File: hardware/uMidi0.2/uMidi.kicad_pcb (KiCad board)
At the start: 2 copper layers, 76.2 x 43.2 mm, 43 parts, among them CON1 USB-MINI-B, IC1 6N138, IC2 ATXMEGA128A4U-M, P1 MIDI In, P2 MIDI Thru, P3 MIDI T/O, P4 MIDI Out, P5 5..12 V, P6 PDI, P7 GPIO1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

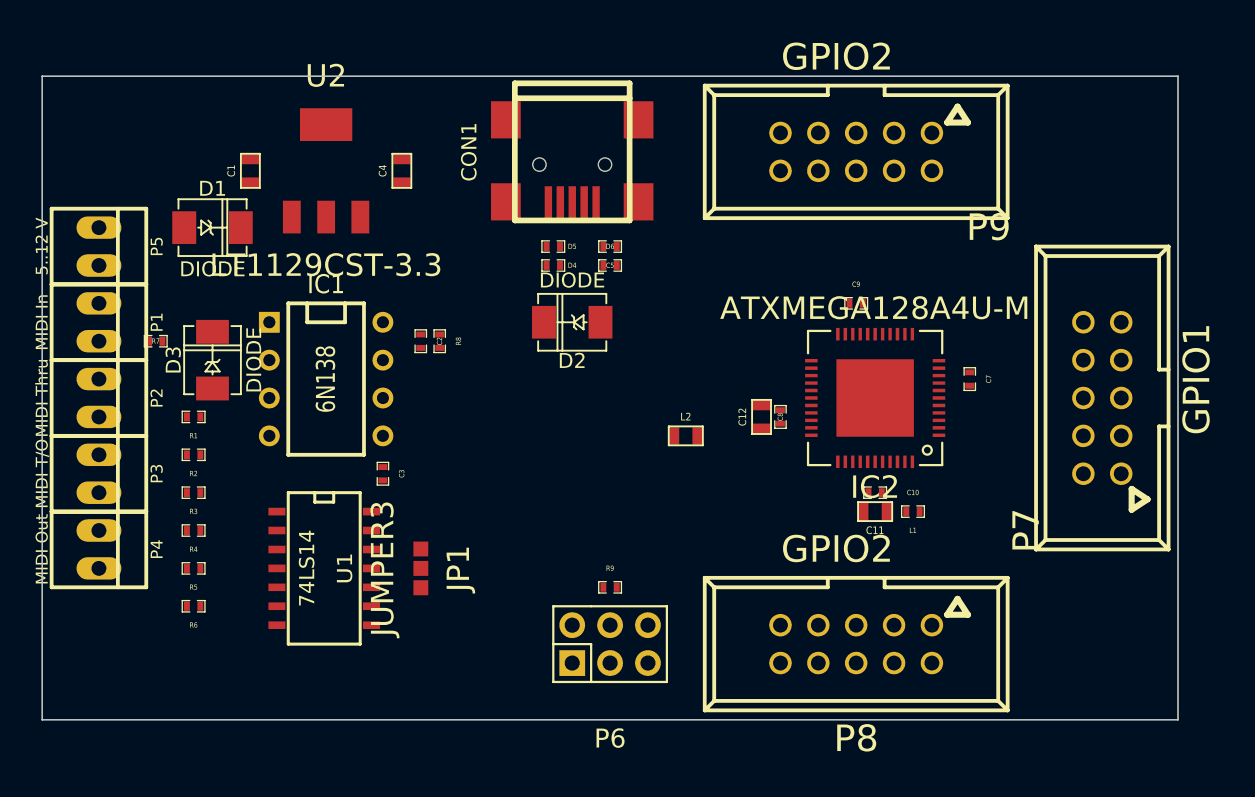
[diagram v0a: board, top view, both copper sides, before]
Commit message: Revise placement, make more compact
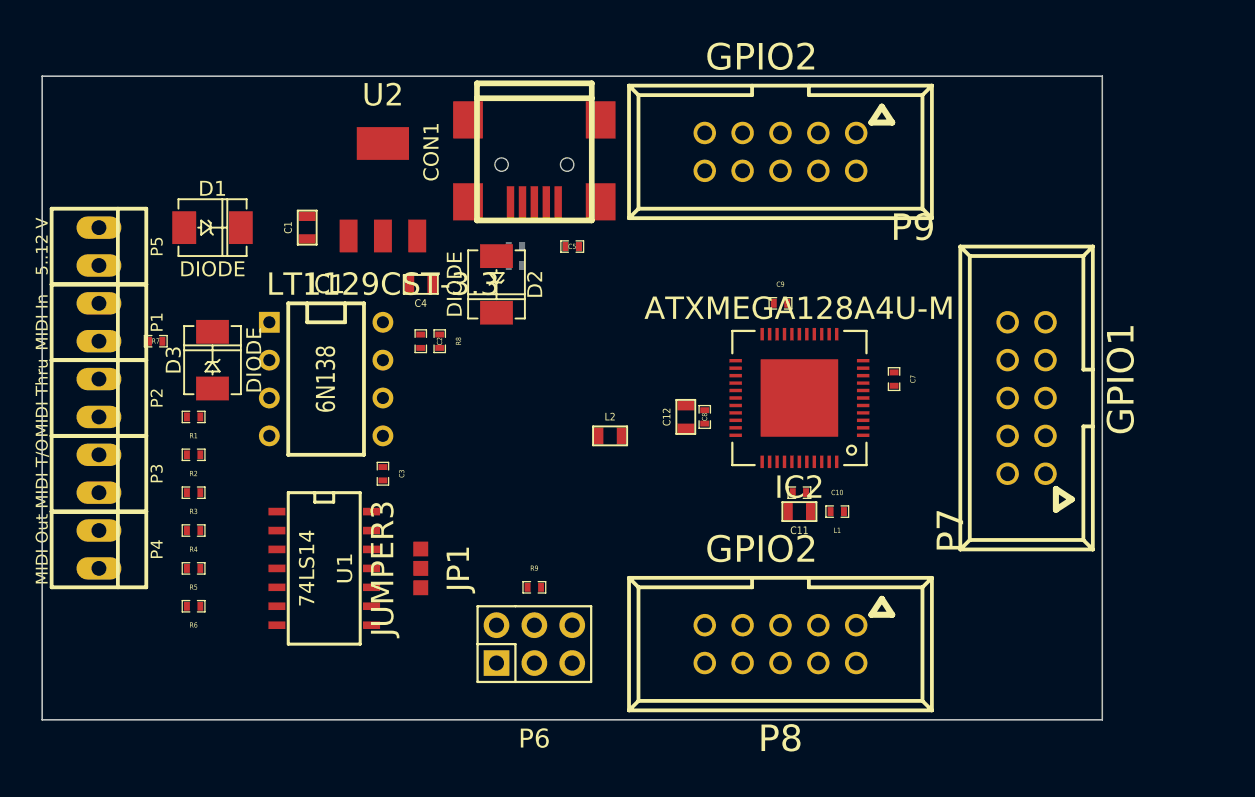
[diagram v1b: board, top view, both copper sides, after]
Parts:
- D4, D5, D6: moved to B.Cu
- moved C4 7.73 mm to (92.7, 135.9), turned to 180 degrees
- moved D2 5.68 mm to (97.8, 135.9), turned to 270 degrees
- moved C1 5.39 mm to (85.1, 132.1)
- moved P7 5.08 mm to (133.3, 143.5)
- moved C10 5.08 mm to (118.1, 149.9)
- moved C11 5.08 mm to (118.1, 151.1)
- moved C12 5.08 mm to (110.5, 144.8)
- moved C7 5.08 mm to (124.5, 142.2)
- moved C8 5.08 mm to (111.8, 144.8)
- moved C9 5.08 mm to (116.8, 137.2)
- moved IC2 5.08 mm to (118.1, 143.5)
- moved L1 5.08 mm to (120.7, 151.1)
- moved L2 5.08 mm to (105.4, 146.1)
- moved P6 5.08 mm to (100.3, 160.0)
- moved P8 5.08 mm to (116.8, 160.0)
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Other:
- board size 76.2 x 43.2 mm -> 71.1 x 43.2 mm

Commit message: Set design rules
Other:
- net class Default: clearance 0.254 -> 0.15; trace_width 0.254 -> 0.15; via_dia 0.889 -> 0.6; via_drill 0.635 -> 0.3
- rule trace_clearance: 0.254 -> 0.15
- rule trace_min: 0.254 -> 0.15
- rule via_min_drill: 0.508 -> 0.3
- rule via_min_size: 0.889 -> 0.6
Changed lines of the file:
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@@
   )
   (setup
-    (last_trace_width 0.254)
-    (trace_clearance 0.254)
+    (last_trace_width 0.15)
+    (trace_clearance 0.15)
     (zone_clearance 0.508)
     (zone_45_only no)
-    (trace_min 0.254)
+    (trace_min 0.15)
     (segment_width 0.2)
     (edge_width 0.1)
-    (via_size 0.889)
-    (via_drill 0.635)
-    (via_min_size 0.889)
-    (via_min_drill 0.508)
+    (via_size 0.6)
+    (via_drill 0.3)
+    (via_min_size 0.6)
+    (via_min_drill 0.3)
     (uvia_size 0.508)
     (uvia_drill 0.127)
@@
   (net 64 "Net-(U1-Pad5)")
   (net_class Default "This is the default net class."
-    (clearance 0.254)
-    (trace_width 0.254)
-    (via_dia 0.889)
-    (via_drill 0.635)
+    (clearance 0.15)
+    (trace_width 0.15)
+    (via_dia 0.6)
+    (via_drill 0.3)
     (uvia_dia 0.508)
     (uvia_drill 0.127)

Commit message: Fix MCU ground pad permanently
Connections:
- net +3.3V renamed VCC
- IC2 pad 45: (no net) -> GND
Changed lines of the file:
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@@
 (kicad_pcb (version 4) (host pcbnew "(2014-09-08 BZR 5122)-product")
   (general
-    (links 119)
-    (no_connects 119)
-    (area 67.259999 121.869999 143.560001 165.150001)
+    (links 120)
+    (no_connects 120)
+    (area 67.259999 121.869999 138.480001 165.150001)
     (thickness 1.6)
     (drawings 4)
@@
   (net 60 "Net-(U1-Pad1)")
   (net 61 "Net-(U1-Pad10)")
-  (net 62 +3.3V)
-  (net 63 "Net-(IC1-Pad7)")
-  (net 64 "Net-(U1-Pad5)")
+  (net 62 "Net-(IC1-Pad7)")
+  (net 63 "Net-(U1-Pad5)")
+  (net 64 VCC)
   (net_class Default "This is the default net class."
     (clearance 0.15)
@@
     (uvia_dia 0.508)
     (uvia_drill 0.127)
-    (add_net +3.3V)
     (add_net GND)
     (add_net "Net-(C1-Pad1)")
@@
     (add_net TXD)
     (add_net VBUS)
+    (add_net VCC)
   )
   (module SMD_Packages:SMD-0603 placed (layer F.Cu)
@@
     (fp_line (start 0.762 0.381) (end 0.254 0.381) (layer F.SilkS) (width 0.07112))
     (pad 1 smd rect (at -0.44958 0 270) (size 0.39878 0.59944) (layers F.Cu F.Paste F.Mask)
-      (net 62 +3.3V))
+      (net 64 VCC))
     (pad 2 smd rect (at 0.44958 0 270) (size 0.39878 0.59944) (layers F.Cu F.Paste F.Mask)
       (net 2 GND))
@@
     (fp_line (start 0.762 0.381) (end 0.254 0.381) (layer F.SilkS) (width 0.07112))
     (pad 1 smd rect (at -0.44958 0 90) (size 0.39878 0.59944) (layers F.Cu F.Paste F.Mask)
-      (net 62 +3.3V))
+      (net 64 VCC))
     (pad 2 smd rect (at 0.44958 0 90) (size 0.39878 0.59944) (layers F.Cu F.Paste F.Mask)
       (net 2 GND))
@@
     (fp_line (start -1.143 0.635) (end -1.143 -0.635) (layer F.SilkS) (width 0.127))
     (pad 1 smd rect (at -0.762 0 180) (size 0.635 1.143) (layers F.Cu F.Paste F.Mask)
-      (net 62 +3.3V))
+      (net 64 VCC))
     (pad 2 smd rect (at 0.762 0 180) (size 0.635 1.143) (layers F.Cu F.Paste F.Mask)
       (net 2 GND))
@@
     (pad 44 smd rect (at -2.5 -4.5 180) (size 0.23 0.84) (drill (offset 0 0.22)) (layers F.Cu F.Paste F.Mask)
       (net 46 "Net-(IC2-Pad44)"))
-    (pad 45 smd rect (at 0 0 180) (size 5.2 5.2) (layers F.Cu F.Paste F.Mask))
+    (pad 45 smd rect (at 0 0 180) (size 5.2 5.2) (layers F.Cu F.Paste F.Mask)
+      (net 2 GND))
   )
   (module Solderjumper:SJ3 placed (layer F.Cu)
@@
     (fp_line (start -1.143 0.635) (end -1.143 -0.635) (layer F.SilkS) (width 0.127))
     (pad 1 smd rect (at -0.762 0) (size 0.635 1.143) (layers F.Cu F.Paste F.Mask)
-      (net 62 +3.3V))
+      (net 64 VCC))
     (pad 2 smd rect (at 0.762 0) (size 0.635 1.143) (layers F.Cu F.Paste F.Mask)
       (net 5 "Net-(C12-Pad1)"))
@@
     (fp_line (start -6.09854 1.9685) (end -7.49808 1.9685) (layer F.SilkS) (width 0.4064))
     (pad 1 thru_hole circle (at -5.08 1.27 90) (size 1.50622 1.50622) (drill 0.99822) (layers *.Cu F.Paste F.SilkS F.Mask)
-      (net 62 +3.3V))
+      (net 64 VCC))
     (pad 2 thru_hole circle (at -5.08 -1.27 90) (size 1.50622 1.50622) (drill 0.99822) (layers *.Cu F.Paste F.SilkS F.Mask)
       (net 42 "Net-(IC2-Pad40)"))
@@
     (fp_line (start -6.09854 1.9685) (end -7.49808 1.9685) (layer F.SilkS) (width 0.4064))
     (pad 1 thru_hole circle (at -5.08 1.27 180) (size 1.50622 1.50622) (drill 0.99822) (layers *.Cu F.Paste F.SilkS F.Mask)
-      (net 62 +3.3V))
+      (net 64 VCC))
     (pad 2 thru_hole circle (at -5.08 -1.27 180) (size 1.50622 1.50622) (drill 0.99822) (layers *.Cu F.Paste F.SilkS F.Mask)
       (net 17 "Net-(IC2-Pad4)"))
@@
     (fp_line (start -6.09854 1.9685) (end -7.49808 1.9685) (layer F.SilkS) (width 0.4064))
     (pad 1 thru_hole circle (at -5.08 1.27 180) (size 1.50622 1.50622) (drill 0.99822) (layers *.Cu F.Paste F.SilkS F.Mask)
-      (net 62 +3.3V))
+      (net 64 VCC))
     (pad 2 thru_hole circle (at -5.08 -1.27 180) (size 1.50622 1.50622) (drill 0.99822) (layers *.Cu F.Paste F.SilkS F.Mask)
       (net 25 "Net-(IC2-Pad14)"))
@@
     (fp_line (start 0.762 0.381) (end 0.254 0.381) (layer F.SilkS) (width 0.07112))
     (pad 1 smd rect (at -0.44958 0 180) (size 0.39878 0.59944) (layers F.Cu F.Paste F.Mask)
-      (net 62 +3.3V))
+      (net 64 VCC))
     (pad 2 smd rect (at 0.44958 0 180) (size 0.39878 0.59944) (layers F.Cu F.Paste F.Mask)
       (net 49 "Net-(P2-Pad1)"))
@@
     (fp_line (start 0.762 0.381) (end 0.254 0.381) (layer F.SilkS) (width 0.07112))
     (pad 1 smd rect (at -0.44958 0 180) (size 0.39878 0.59944) (layers F.Cu F.Paste F.Mask)
-      (net 62 +3.3V))
+      (net 64 VCC))
     (pad 2 smd rect (at 0.44958 0 180) (size 0.39878 0.59944) (layers F.Cu F.Paste F.Mask)
       (net 51 "Net-(P3-Pad1)"))
@@
     (fp_line (start 0.762 0.381) (end 0.254 0.381) (layer F.SilkS) (width 0.07112))
     (pad 1 smd rect (at -0.44958 0 180) (size 0.39878 0.59944) (layers F.Cu F.Paste F.Mask)
-      (net 62 +3.3V))
+      (net 64 VCC))
     (pad 2 smd rect (at 0.44958 0 180) (size 0.39878 0.59944) (layers F.Cu F.Paste F.Mask)
       (net 53 "Net-(P4-Pad1)"))
@@
       (net 13 RXD))
     (pad 2 smd rect (at 0.44958 0 90) (size 0.39878 0.59944) (layers F.Cu F.Paste F.Mask)
-      (net 62 +3.3V))
+      (net 64 VCC))
     (model smd\chip_cms.wrl
       (at (xyz 0 0 0.002))
@@
       (net 58 "Net-(R4-Pad1)"))
     (pad 5 smd rect (at 1.27 3.302 270) (size 0.508 1.143) (layers F.Cu F.Paste F.Mask)
-      (net 64 "Net-(U1-Pad5)"))
+      (net 63 "Net-(U1-Pad5)"))
     (pad 6 smd rect (at 2.54 3.302 270) (size 0.508 1.143) (layers F.Cu F.Paste F.Mask)
       (net 59 "Net-(R6-Pad1)"))
@@
       (net 2 GND))
     (pad 8 smd rect (at 3.81 -3.048 270) (size 0.508 1.143) (layers F.Cu F.Paste F.Mask)
-      (net 64 "Net-(U1-Pad5)"))
+      (net 63 "Net-(U1-Pad5)"))
     (pad 9 smd rect (at 2.54 -3.048 270) (size 0.508 1.143) (layers F.Cu F.Paste F.Mask)
       (net 37 TXD))
@@
       (net 13 RXD))
     (pad 14 smd rect (at -3.81 -3.048 270) (size 0.508 1.143) (layers F.Cu F.Paste F.Mask)
-      (net 62 +3.3V))
+      (net 64 VCC))
     (pad 10 smd rect (at 1.27 -3.048 270) (size 0.508 1.143) (layers F.Cu F.Paste F.Mask)
       (net 61 "Net-(U1-Pad10)"))
@@
       (net 2 GND))
     (pad 3 smd rect (at 2.3 3.1) (size 1.2 2.2) (layers F.Cu F.Paste F.Mask)
-      (net 62 +3.3V))
+      (net 64 VCC))
     (pad 4 smd rect (at 0 -3.1) (size 3.5 2.2) (layers F.Cu F.Paste F.Mask)
       (net 2 GND))
@@
       (net 13 RXD))
     (pad 7 thru_hole circle (at -1.27 -3.81 270) (size 1.397 1.397) (drill 0.8128) (layers *.Cu *.Mask F.SilkS)
-      (net 63 "Net-(IC1-Pad7)"))
+      (net 62 "Net-(IC1-Pad7)"))
     (pad 8 thru_hole circle (at -3.81 -3.81 270) (size 1.397 1.397) (drill 0.8128) (layers *.Cu *.Mask F.SilkS)
-      (net 62 +3.3V))
+      (net 64 VCC))
     (model dil/dil_8.wrl
       (at (xyz 0 0 0))

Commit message: Create design rule for power signals
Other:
- net class Power added: clearance 0.15, trace_width 0.3, via_dia 0.6, via_drill 0.3
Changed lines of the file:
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@@
     (links 120)
     (no_connects 120)
-    (area 67.259999 121.869999 138.480001 165.150001)
+    (area 64.230952 119.07205 143.923784 167.85905)
     (thickness 1.6)
     (drawings 4)
@@
     (uvia_dia 0.508)
     (uvia_drill 0.127)
-    (add_net GND)
-    (add_net "Net-(C1-Pad1)")
     (add_net "Net-(C10-Pad1)")
     (add_net "Net-(C12-Pad1)")
@@
     (add_net "Net-(CON1-Pad4)")
     (add_net "Net-(CON1-Pad6)")
-    (add_net "Net-(D1-Pad1)")
     (add_net "Net-(D3-Pad1)")
     (add_net "Net-(D3-Pad2)")
@@
     (add_net RXD)
     (add_net TXD)
+  )
+  (net_class Power ""
+    (clearance 0.15)
+    (trace_width 0.3)
+    (via_dia 0.6)
+    (via_drill 0.3)
+    (uvia_dia 0.508)
+    (uvia_drill 0.127)
+    (add_net GND)
+    (add_net "Net-(C1-Pad1)")
+    (add_net "Net-(D1-Pad1)")
     (add_net VBUS)
     (add_net VCC)

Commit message: Route; Optimze placement
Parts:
- D4, D5, D6: moved to F.Cu
- JP1: moved to B.Cu
- moved P7 23.3 mm to (116.8, 160.0), turned to 0 degrees
- moved P8 23.3 mm to (133.3, 143.5), turned to 90 degrees
- moved R9 14.4 mm to (113.3, 149.9)
- moved L1 7.37 mm to (113.3, 151.4), turned to 0 degrees
- moved D4 6.53 mm to (104.9, 137.5), turned to 90 degrees
- moved D5 6.07 mm to (104.9, 135.0), turned to 270 degrees
- moved C5 4.74 mm to (98.2, 132.7)
- moved C3 3.25 mm to (92.2, 151.1), turned to 0 degrees
- moved R7 3.17 mm to (76.8, 137.2)
- moved C11 2.71 mm to (115.4, 150.6), turned to 90 degrees
- moved L2 2.40 mm to (107.4, 144.8), turned to 270 degrees
- moved R1 1.80 mm to (78.7, 146.1)
- moved R2 1.80 mm to (78.7, 148.6)
- moved R5 1.80 mm to (78.7, 156.2)
- moved R6 1.80 mm to (78.7, 158.8)
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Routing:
- net GND: track 0.00 -> 32.8 mm
- net TXD: track 0.00 -> 30.4 mm, vias 0 -> 2
- net Net-(C12-Pad1): track 0.00 -> 27.3 mm
- net Net-(IC2-Pad34): track 0.00 -> 26.3 mm
- net Net-(CON1-Pad3): track 0.00 -> 21.3 mm
- net Net-(IC2-Pad3): track 0.00 -> 21.1 mm
- net Net-(IC2-Pad35): track 0.00 -> 21.0 mm
- net Net-(CON1-Pad2): track 0.00 -> 20.4 mm
- net Net-(IC2-Pad1): track 0.00 -> 17.7 mm
- net Net-(IC2-Pad2): track 0.00 -> 16.9 mm
- net Net-(IC2-Pad13): track 0.00 -> 16.6 mm
- net Net-(IC2-Pad41): track 0.00 -> 16.3 mm
- net Net-(IC2-Pad23): track 0.00 -> 16.0 mm
- net Net-(IC2-Pad43): track 0.00 -> 15.7 mm
- net Net-(IC2-Pad21): track 0.00 -> 14.6 mm
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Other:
- net class USB added: clearance 0.15, trace_width 0.3, via_dia 0.6, via_drill 0.3
